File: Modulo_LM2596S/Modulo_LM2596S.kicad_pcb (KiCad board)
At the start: 2 copper layers, 48.8 x 26.6 mm, 21 parts, among them J101 Conn_01x01_Female, J102 Conn_01x01_Female, J103 Conn_01x01_Female, J104 Conn_01x01_Female, J105 Conn_01x01_Female, J106 Conn_01x01_Female, J107 Conn_01x01_Female, J108 Conn_01x01_Female, U101 LM2596S-ADJ

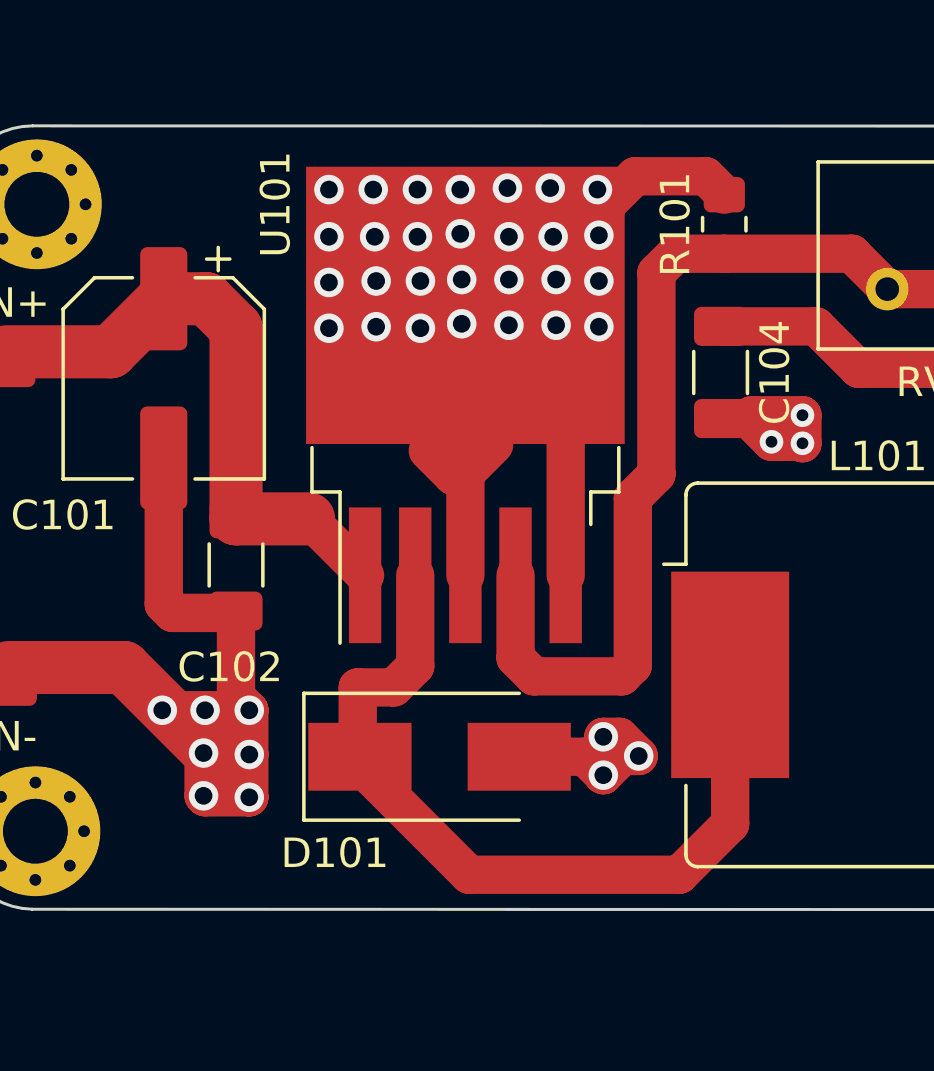
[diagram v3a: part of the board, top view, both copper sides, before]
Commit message: LM2596S: Ordine della scheda da JLCPCB
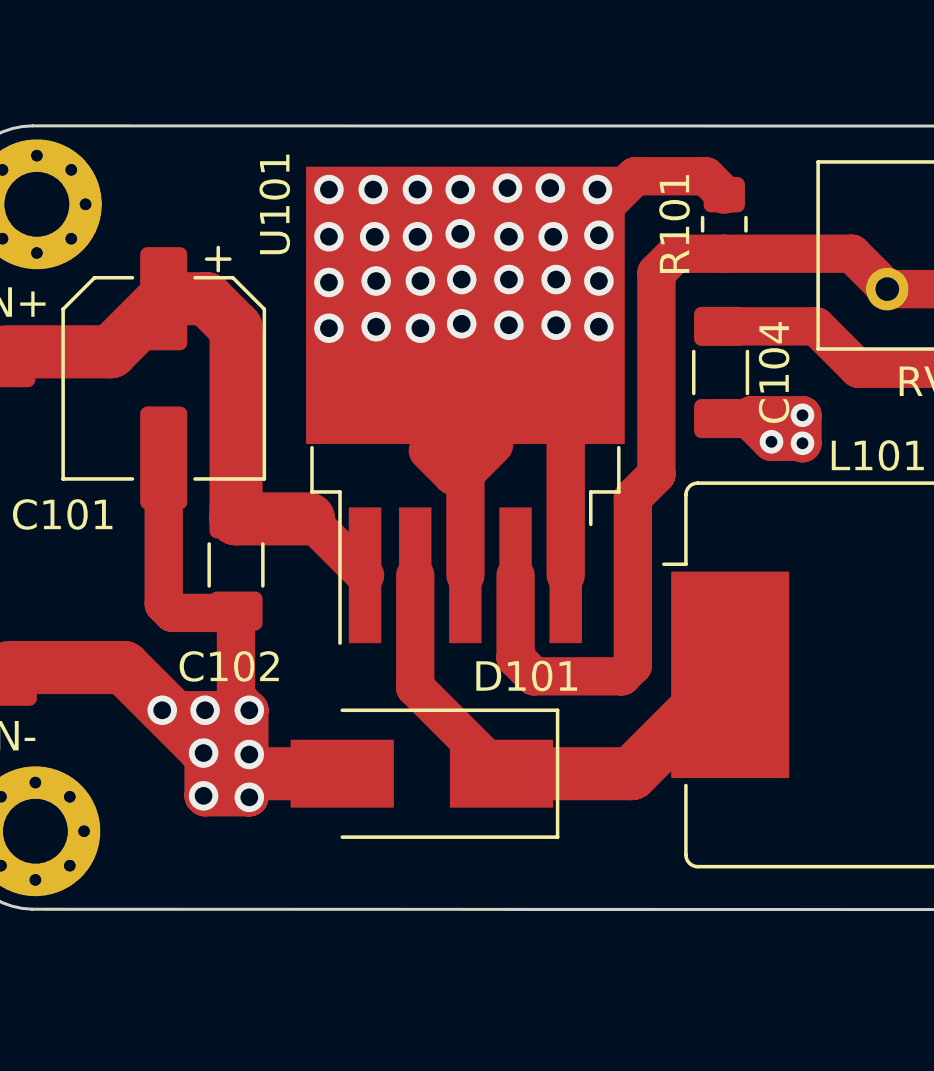
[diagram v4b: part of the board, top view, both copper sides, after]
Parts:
- moved D101 0.83 mm to (167.7, 90.5), turned to 180 degrees
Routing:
- net Net-(D101-Pad1): track 27.9 -> 17.1 mm
- net OUT-: track 99.7 -> 97.5 mm, vias 47 -> 44
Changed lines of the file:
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@@
       (outputformat 1)
       (mirror false)
-      (drillshape 1)
+      (drillshape 0)
       (scaleselection 1)
-      (outputdirectory "")
+      (outputdirectory "gerber/")
     )
   )
@@
     (fp_line (start 1.6 0.8) (end -1.6 0.8) (layer "F.Fab") (width 0.1))
     (fp_line (start -1.6 0.8) (end -1.6 -0.8) (layer "F.Fab") (width 0.1))
-    (pad "1" smd roundrect (at -1.5625 0 270) (size 1.325 1.8) (layers "F.Cu" "F.Paste" "F.Mask") (roundrect_rratio 0.188679)
+    (pad "1" smd roundrect (at -1.5625 0 270) (size 1.325 1.8) (layers "F.Cu" "F.Paste" "F.Mask") (roundrect_rratio 0.1886792453)
       (net 1 "Vin+") (pintype "passive"))
-    (pad "2" smd roundrect (at 1.5625 0 270) (size 1.325 1.8) (layers "F.Cu" "F.Paste" "F.Mask") (roundrect_rratio 0.188679)
+    (pad "2" smd roundrect (at 1.5625 0 270) (size 1.325 1.8) (layers "F.Cu" "F.Paste" "F.Mask") (roundrect_rratio 0.1886792453)
       (net 3 "OUT-") (pintype "passive"))
     (model "${KICAD6_3DMODEL_DIR}/Capacitor_SMD.3dshapes/C_1206_3216Metric.wrl"
@@
     (fp_line (start -1 -0.625) (end 1 -0.625) (layer "F.Fab") (width 0.1))
     (fp_line (start 1 -0.625) (end 1 0.625) (layer "F.Fab") (width 0.1))
-    (pad "1" smd roundrect (at -1 0 90) (size 1.2 1.4) (layers "F.Cu" "F.Paste" "F.Mask") (roundrect_rratio 0.208333)
+    (pad "1" smd roundrect (at -1 0 90) (size 1.2 1.4) (layers "F.Cu" "F.Paste" "F.Mask") (roundrect_rratio 0.2083333333)
       (net 2 "Net-(R101-Pad1)") (pintype "passive"))
-    (pad "2" smd roundrect (at 1 0 90) (size 1.2 1.4) (layers "F.Cu" "F.Paste" "F.Mask") (roundrect_rratio 0.208333)
+    (pad "2" smd roundrect (at 1 0 90) (size 1.2 1.4) (layers "F.Cu" "F.Paste" "F.Mask") (roundrect_rratio 0.2083333333)
       (net 3 "OUT-") (pintype "passive"))
     (model "${KICAD6_3DMODEL_DIR}/Resistor_SMD.3dshapes/R_0805_2012Metric.wrl"
@@
     (fp_line (start -1.6 -0.8) (end 1.6 -0.8) (layer "F.Fab") (width 0.1))
     (fp_line (start 1.6 0.8) (end -1.6 0.8) (layer "F.Fab") (width 0.1))
-    (pad "1" smd roundrect (at -1.5625 0 270) (size 1.325 1.8) (layers "F.Cu" "F.Paste" "F.Mask") (roundrect_rratio 0.188679)
+    (pad "1" smd roundrect (at -1.5625 0 270) (size 1.325 1.8) (layers "F.Cu" "F.Paste" "F.Mask") (roundrect_rratio 0.1886792453)
       (net 4 "OUT+") (pintype "passive"))
-    (pad "2" smd roundrect (at 1.5625 0 270) (size 1.325 1.8) (layers "F.Cu" "F.Paste" "F.Mask") (roundrect_rratio 0.188679)
+    (pad "2" smd roundrect (at 1.5625 0 270) (size 1.325 1.8) (layers "F.Cu" "F.Paste" "F.Mask") (roundrect_rratio 0.1886792453)
       (net 3 "OUT-") (pintype "passive"))
     (model "${KICAD6_3DMODEL_DIR}/Capacitor_SMD.3dshapes/C_1206_3216Metric.wrl"
@@
   )
   (footprint "Diode_SMD:D_SMB_Handsoldering" (layer "F.Cu")
-    (at 168.25 89.875)
+    (at 167.65 90.45 180)
     (descr "Diode SMB (DO-214AA) Handsoldering")
     (tags "Diode SMB (DO-214AA) Handsoldering")
@@
     (fp_line (start -0.64944 0.00102) (end 0.50118 0.75032) (layer "F.Fab") (width 0.1))
     (fp_line (start -0.64944 -0.79908) (end -0.64944 0.80112) (layer "F.Fab") (width 0.1))
-    (pad "1" smd rect (at -2.7 0) (size 3.5 2.3) (layers "F.Cu" "F.Paste" "F.Mask")
+    (pad "1" smd rect (at -2.7 0 180) (size 3.5 2.3) (layers "F.Cu" "F.Paste" "F.Mask")
       (net 5 "Net-(D101-Pad1)") (pinfunction "K") (pintype "passive"))
-    (pad "2" smd rect (at 2.7 0) (size 3.5 2.3) (layers "F.Cu" "F.Paste" "F.Mask")
+    (pad "2" smd rect (at 2.7 0 180) (size 3.5 2.3) (layers "F.Cu" "F.Paste" "F.Mask")
       (net 3 "OUT-") (pinfunction "A") (pintype "passive"))
     (model "${KICAD6_3DMODEL_DIR}/Diode_SMD.3dshapes/D_SMB.wrl"
@@
   (segment (start 157.55 86.85) (end 160.25 89.55) (width 1.8) (layer "F.Cu") (net 3))
   (segment (start 158.9 84.7) (end 159.2 85) (width 1.3) (layer "F.Cu") (net 3))
-  (segment (start 175 89.85) (end 174.45 89.85) (width 1.3) (layer "F.Cu") (net 3))
   (segment (start 167.85 79.5) (end 168.7 80.35) (width 1.3) (layer "F.Cu") (net 3))
   (segment (start 172.525 83.725) (end 172.525 77.975) (width 1.3) (layer "F.Cu") (net 3))
@@
   (segment (start 160.25 89.75) (end 160.25 91.2) (width 1.3) (layer "F.Cu") (net 3))
   (segment (start 198.7 88.2) (end 194.55 88.2) (width 1.8) (layer "F.Cu") (net 3))
+  (segment (start 164.95 90.45) (end 161.15 90.45) (width 1.8) (layer "F.Cu") (net 3))
   (segment (start 180.55 78.3) (end 178.825 78.3) (width 1.3) (layer "F.Cu") (net 3))
-  (segment (start 174.35 89.2) (end 175 89.85) (width 1.3) (layer "F.Cu") (net 3))
   (segment (start 180.55 78.3) (end 180.55 79.25) (width 1.3) (layer "F.Cu") (net 3))
   (segment (start 194.6 86.45) (end 194.6 88.15) (width 1.8) (layer "F.Cu") (net 3))
@@
   (segment (start 161.5 88.3) (end 160.25 89.55) (width 1.3) (layer "F.Cu") (net 3))
   (segment (start 191.75 88.65) (end 194.1 88.65) (width 1.8) (layer "F.Cu") (net 3))
-  (segment (start 173.175 89.875) (end 173.8 90.5) (width 1.3) (layer "F.Cu") (net 3))
-  (segment (start 173.8 89.2) (end 174.35 89.2) (width 1.3) (layer "F.Cu") (net 3))
   (segment (start 160.25 88.35) (end 160.3 88.3) (width 1.3) (layer "F.Cu") (net 3))
-  (segment (start 174.45 89.85) (end 173.8 90.5) (width 1.3) (layer "F.Cu") (net 3))
   (segment (start 160.25 89.75) (end 160.3 89.75) (width 1.3) (layer "F.Cu") (net 3))
   (segment (start 159.2 85) (end 161.2875 85) (width 1.3) (layer "F.Cu") (net 3))
@@
   (segment (start 160.25 89.75) (end 161.75 89.75) (width 1.3) (layer "F.Cu") (net 3))
   (segment (start 174.875 70.2) (end 177.275 70.2) (width 1.3) (layer "F.Cu") (net 3))
-  (segment (start 170.95 89.875) (end 173.175 89.875) (width 1.3) (layer "F.Cu") (net 3))
   (segment (start 168.7 80.35) (end 169.125 80.35) (width 1.3) (layer "F.Cu") (net 3))
   (segment (start 161.75 89.75) (end 161.8 89.8) (width 1.3) (layer "F.Cu") (net 3))
+  (segment (start 161.15 90.45) (end 160.25 89.55) (width 1.8) (layer "F.Cu") (net 3))
   (segment (start 172.925 72.15) (end 174.875 70.2) (width 1.3) (layer "F.Cu") (net 3))
   (segment (start 158.85 88.3) (end 158.85 88.35) (width 1.3) (layer "F.Cu") (net 3))
   (segment (start 161.8 88.3) (end 161.8 89.8) (width 1.3) (layer "F.Cu") (net 3))
-  (segment (start 173.8 90.5) (end 173.8 89.2) (width 1.3) (layer "F.Cu") (net 3))
   (segment (start 194.6 85.15) (end 194.6 86.45) (width 1.8) (layer "F.Cu") (net 3))
   (segment (start 177.275 70.2) (end 177.9 70.825) (width 1.3) (layer "F.Cu") (net 3))
@@
   (via (at 160.3 88.3) (size 1) (drill 0.6) (layers "F.Cu" "B.Cu") (net 3))
   (via (at 180.55 78.3) (size 0.8) (drill 0.4) (layers "F.Cu" "B.Cu") (net 3))
-  (via (at 173.8 90.5) (size 1) (drill 0.6) (layers "F.Cu" "B.Cu") (net 3))
   (via (at 172.2 73.7) (size 1) (drill 0.6) (layers "F.Cu" "B.Cu") (net 3))
   (via (at 160.25 89.75) (size 1) (drill 0.6) (layers "F.Cu" "B.Cu") (net 3))
@@
   (via (at 191.75 88.65) (size 0.8) (drill 0.4) (layers "F.Cu" "B.Cu") (net 3))
   (via (at 180.55 79.25) (size 0.8) (drill 0.4) (layers "F.Cu" "B.Cu") (net 3))
-  (via (at 173.8 89.2) (size 1) (drill 0.6) (layers "F.Cu" "B.Cu") (net 3))
   (via (at 160.25 91.2) (size 1) (drill 0.6) (layers "F.Cu" "B.Cu") (net 3))
   (via (at 164.5 75.35) (size 1) (drill 0.6) (layers "F.Cu" "B.Cu") (net 3))
   (via (at 166.1 75.3) (size 1) (drill 0.6) (layers "F.Cu" "B.Cu") (net 3))
-  (via (at 175 89.85) (size 1) (drill 0.6) (layers "F.Cu" "B.Cu") (net 3))
   (via (at 161.8 91.25) (size 1) (drill 0.6) (layers "F.Cu" "B.Cu") (net 3))
   (via (at 166 70.65) (size 1) (drill 0.6) (layers "F.Cu" "B.Cu") (net 3))
@@
   (segment (start 188.1 82.05) (end 192.3 82.05) (width 1.3) (layer "F.Cu") (net 4))
   (segment (start 188.505 75.195) (end 188.505 74.025) (width 1.3) (layer "F.Cu") (net 4))
-  (segment (start 167.425 83.725) (end 167.425 86.8) (width 1.3) (layer "F.Cu") (net 5))
-  (segment (start 165.475 87.525) (end 165.475 89.8) (width 1.3) (layer "F.Cu") (net 5))
-  (segment (start 165.475 89.8) (end 165.55 89.875) (width 1.3) (layer "F.Cu") (net 5))
-  (segment (start 178.1 92.15) (end 178.1 87.1) (width 1.3) (layer "F.Cu") (net 5))
-  (segment (start 169.25 93.875) (end 176.375 93.875) (width 1.3) (layer "F.Cu") (net 5))
-  (segment (start 165.55 90.175) (end 169.25 93.875) (width 1.3) (layer "F.Cu") (net 5))
-  (segment (start 166.7 87.525) (end 165.475 87.525) (width 1.3) (layer "F.Cu") (net 5))
-  (segment (start 165.55 89.875) (end 165.55 90.175) (width 1.3) (layer "F.Cu") (net 5))
-  (segment (start 167.425 86.8) (end 166.7 87.525) (width 1.3) (layer "F.Cu") (net 5))
-  (segment (start 176.375 93.875) (end 178.1 92.15) (width 1.3) (layer "F.Cu") (net 5))
+  (segment (start 170.35 90.45) (end 174.75 90.45) (width 1.8) (layer "F.Cu") (net 5))
+  (segment (start 167.425 83.725) (end 167.425 87.525) (width 1.3) (layer "F.Cu") (net 5))
+  (segment (start 174.75 90.45) (end 178.1 87.1) (width 1.8) (layer "F.Cu") (net 5))
+  (segment (start 167.425 87.525) (end 170.35 90.45) (width 1.3) (layer "F.Cu") (net 5))
   (zone (net 3) (net_name "OUT-") (layer "B.Cu") (hatch edge 0.508)
     (connect_pads (clearance 0.508))
